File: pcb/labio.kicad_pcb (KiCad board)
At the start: 2 copper layers, 150 x 85 mm, 212 parts, among them IC201 AT24CS32-XHM, J701 JACK_TRRS_6PINS, P1 CONN_02X20, P301 CONN_01X04, P302 CONN_01X04, P303 CONN_01X04, P401 CONN_01X12, P601 CONN_01X02, P602 CONN_01X02, P603 CONN_01X04, P604 CONN_01X02, P605 CONN_01X03, P606 CONN_01X03, P607 CONN_01X05, P608 CONN_01X05, P701 CONN_01X04, P702 CONN_01X04, P703 CONN_01X04, P704 CONN_01X02, P901 CONN_01X06, Q301 PHOTOTRANSISTOR, Q302 Q_NMOS_GSD, Q303 Q_NMOS_GSD, Q601 Q_NMOS_GSD, Q602 Q_NMOS_GSD, Q603 Q_NMOS_GSD, Q604 Q_NMOS_GSD, Q605 Q_NMOS_GSD, Q606 Q_NMOS_GSD, Q607 Q_NMOS_GSD, Q608 Q_NMOS_GSD, Q609 Q_NMOS_GSD, Q610 Q_NMOS_GSD, Q611 Q_NMOS_GSD, Q612 Q_NMOS_GSD, Q613 Q_NMOS_GSD, SW301 DIP_SWITCH_X04, SW401 DIP_SWITCH_X04, SW501 DIP_SWITCH_X04, SW601 DIP_SWITCH_X04, SW602 DIP_SWITCH_X04, SW603 DIP_SWITCH_X04, SW604 DIP_SWITCH_X04, SW605 ROT_ENC, SW606 DIP_SWITCH_X04, SW701 DIP_SWITCH_X04, SW702 DIP_SWITCH_X04, SW801 SW_PUSH, SW802 SW_PUSH, SW803 SW_PUSH, SW804 SW_PUSH, SW805 SW_PUSH, U201 AP7365_SOT-23-5, U301 ADS1015, U501 LSM303D, U502 BMP280, U503 L3GD20H, U601 L298P_PowerSO20, U701 SPU0410HR5H, U702 WM8731

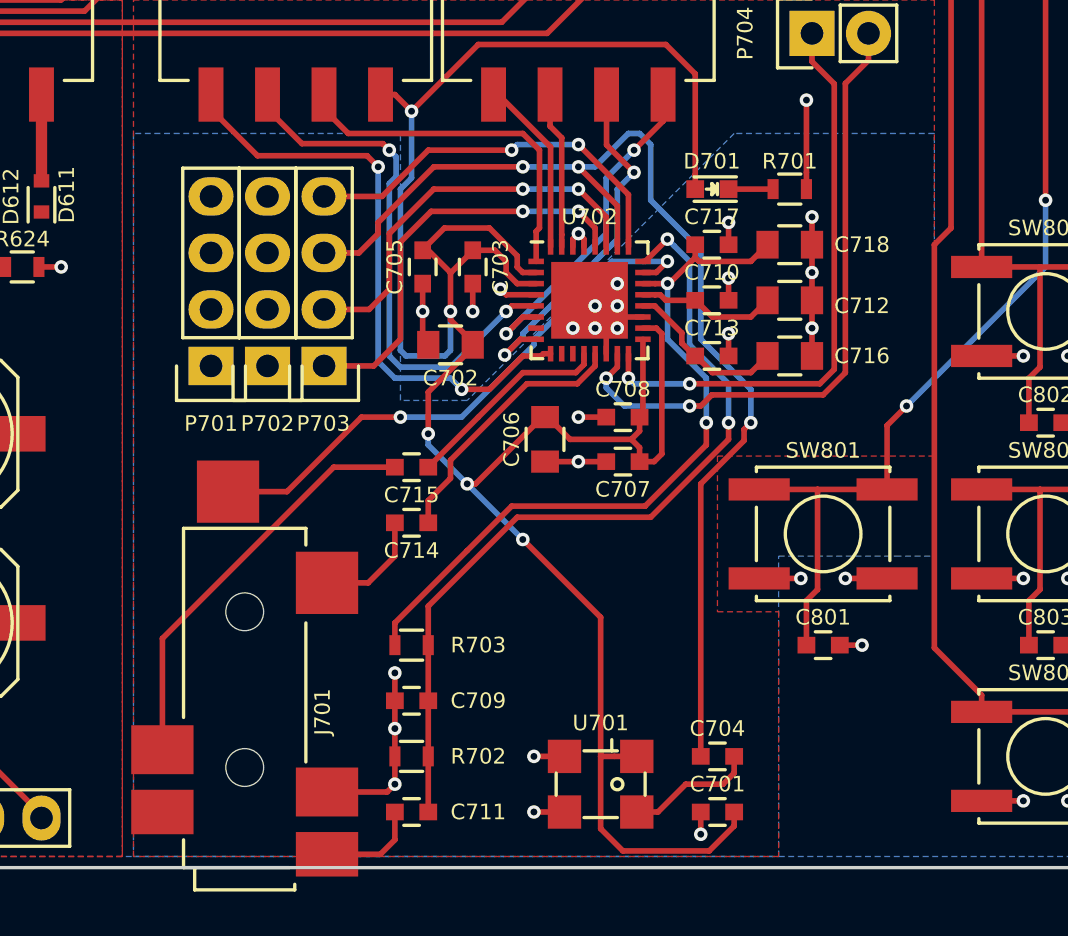
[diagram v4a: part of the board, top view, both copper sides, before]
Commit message: combine gnd and gnda nets per mixed signal layout suggestions from analog, ti
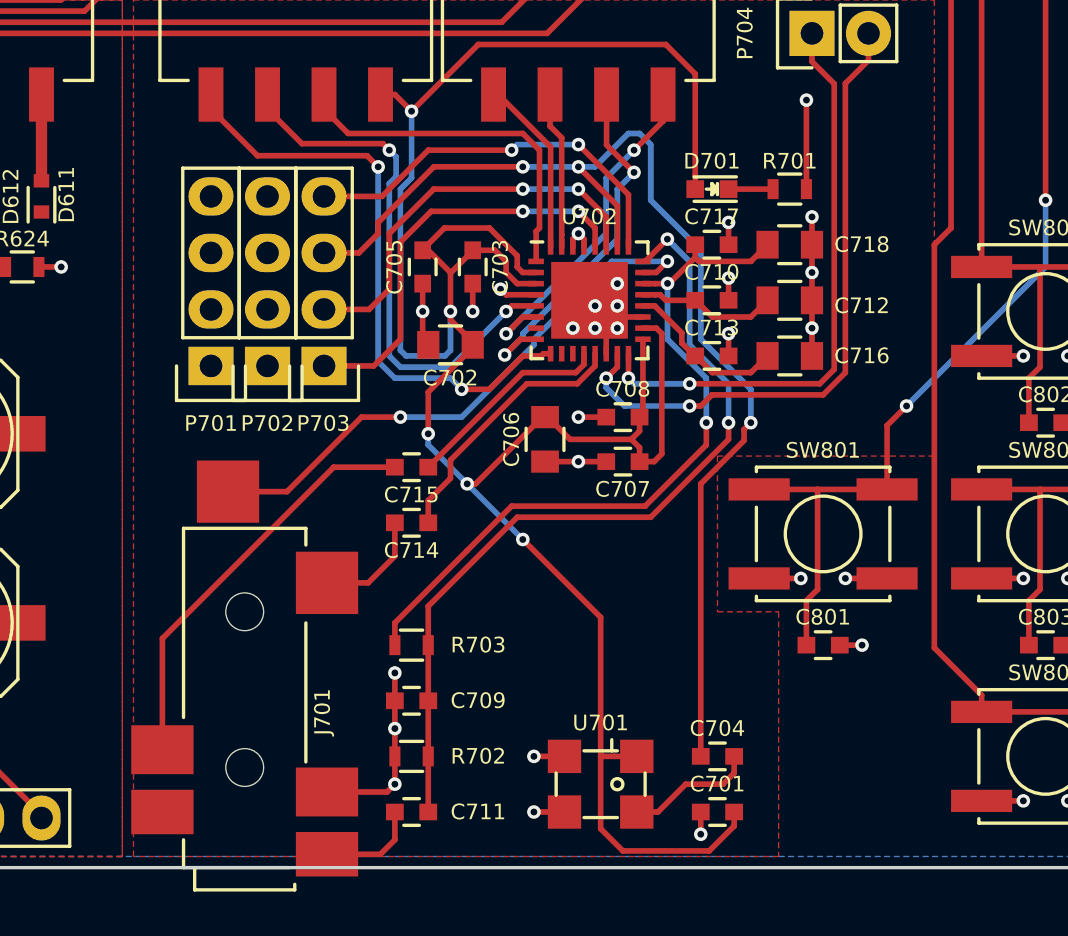
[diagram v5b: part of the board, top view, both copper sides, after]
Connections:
- C701 pad 1: GNDA -> GND
- C706 pad 2: GNDA -> GND
- C707 pad 2: GNDA -> GND
- C708 pad 2: GNDA -> GND
- C709 pad 2: GNDA -> GND
- C710 pad 2: GNDA -> GND
- C712 pad 2: GNDA -> GND
- C713 pad 2: GNDA -> GND
- C716 pad 2: GNDA -> GND
- C717 pad 2: GNDA -> GND
- C718 pad 2: GNDA -> GND
- J701 pad 4: GNDA -> GND
- P701 pad 1: GNDA -> GND
- P701 pad 2: GNDA -> GND
- P701 pad 3: GNDA -> GND
- P701 pad 4: GNDA -> GND
- R702 pad 2: GNDA -> GND
- U701 pad 2: GNDA -> GND
- U701 pad 3: GNDA -> GND
- U702 pad 14: GNDA -> GND
- U702 pad 19: GNDA -> GND
- U702 pad 33: GNDA -> GND
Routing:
- net GND: track 270.7 -> 309.2 mm, vias 181 -> 201
- net GNDA: track 38.5 -> 0.00 mm, vias 20 -> 0
- removed copper zone on B.Cu, net GNDA

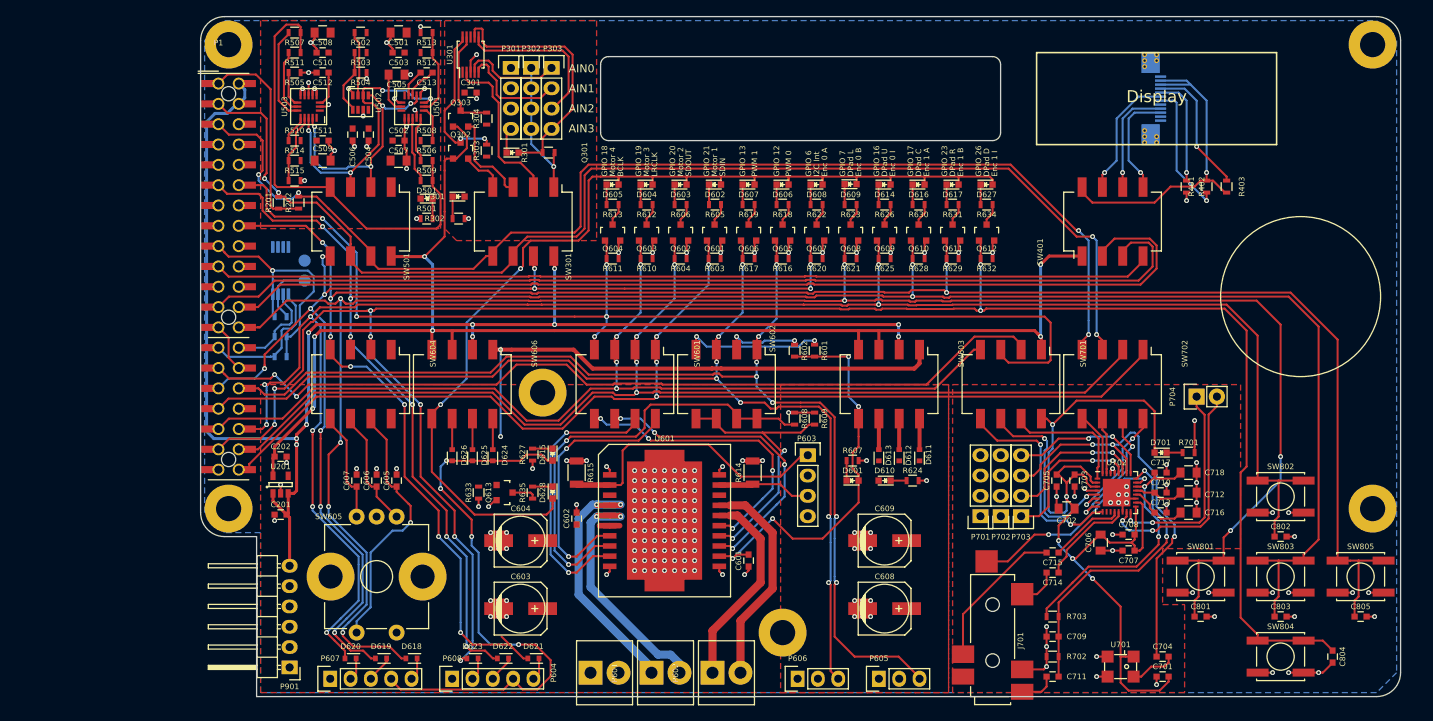
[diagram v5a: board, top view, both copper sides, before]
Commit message: expand outline to 175x85mm. move screen zif connector to top
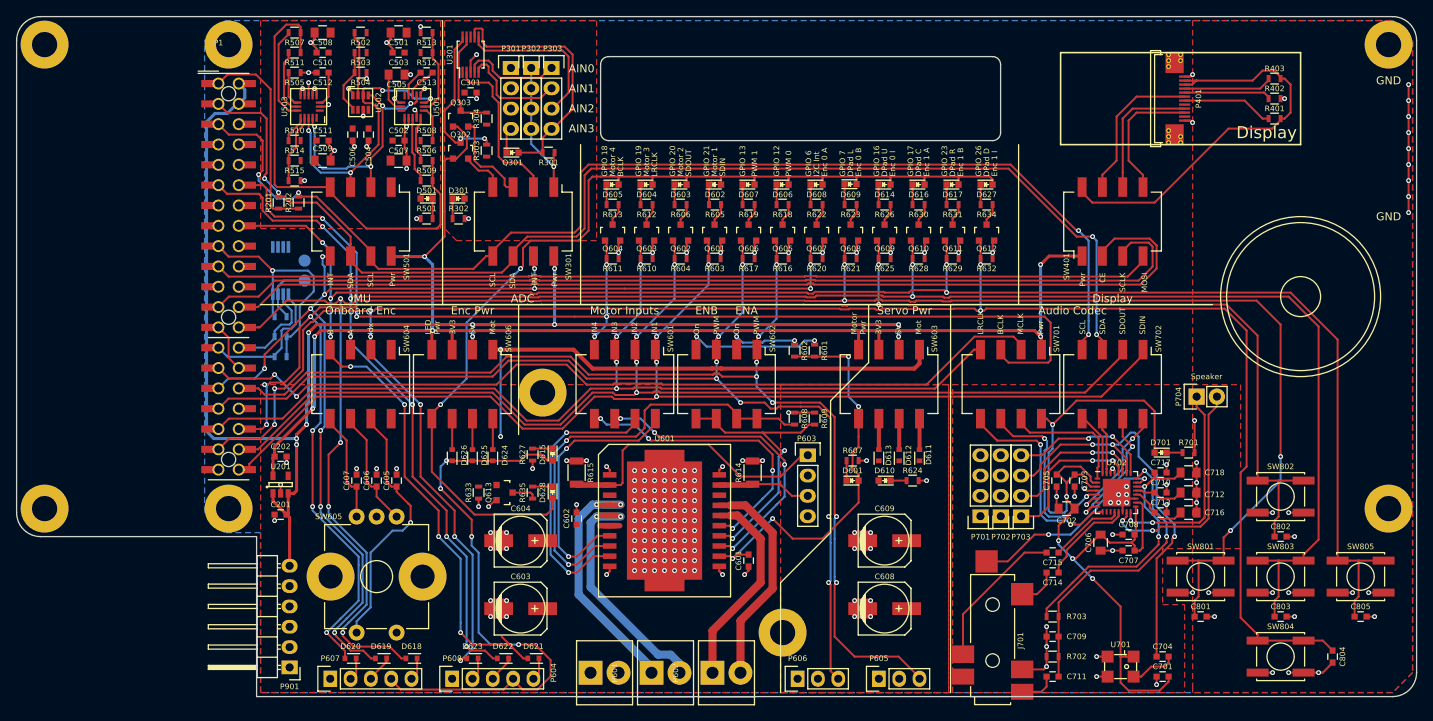
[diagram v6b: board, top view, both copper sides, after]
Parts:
- added H1007: hole, labio-special:hole-m3, F.Cu at (80.5, 53.5)
- added H1008: hole, labio-special:hole-m3, F.Cu at (80.5, 111.5)
- P401: value CONN_01X12 -> SFV12R-1ST__HLF; moved to F.Cu
- moved R402 15.6 mm to (234.2, 60.2), turned to 0 degrees
- moved R403 14.8 mm to (234.2, 57.8), turned to 0 degrees
- moved R401 12.0 mm to (234.2, 62.8), turned to 0 degrees
- moved P401 3.00 mm to (223.0, 60.2), turned to 270 degrees
- moved H1003 2.00 mm to (248.5, 53.5)
- moved H1004 2.00 mm to (248.5, 111.5)
- moved D301 0.25 mm to (132.2, 72.8)
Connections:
- P401 pad 10: Net-(P401-Pad10) -> /labio-display/OLED_MOSI
- P401 pad 11: Net-(P401-Pad10) -> (no net)
- P401 pad 2: (no net) -> Net-(P401-Pad2)
- P401 pad 3: /labio-display/OLED_MOSI -> Net-(P401-Pad2)
- P401 pad 4: /labio-display/OLED_SCK -> /labio-display/OLED_BS0
- P401 pad 5: (no net) -> /labio-display/OLED_BS1
- P401 pad 6: /labio-display/~OLED_RES -> /labio-display/~OLED_CS
- P401 pad 7: /labio-display/~OLED_CS -> /labio-display/~OLED_RES
- P401 pad 8: /labio-display/OLED_BS1 -> (no net)
- P401 pad 9: /labio-display/OLED_BS0 -> /labio-display/OLED_SCK
- R401 pad 2: Net-(P401-Pad10) -> Net-(P401-Pad2)
- R403 pad 2: Net-(P401-Pad10) -> Net-(P401-Pad2)
- SW401 pad 8: Net-(P401-Pad10) -> Net-(P401-Pad2)
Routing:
- net Net-(P401-Pad2): track 0.00 -> 51.9 mm
- net Net-(P401-Pad10): track 41.6 -> 0.00 mm, vias 1 -> 0
- net (no net): track 0.00 -> 16.0 mm, vias 0 -> 9
- net /labio-display/OLED_BS0: track 16.7 -> 11.1 mm, vias 1 -> 0
- net /labio-display/~OLED_RES: track 16.9 -> 11.4 mm, vias 1 -> 0
- net /labio-display/~OLED_CS: track 15.9 -> 19.1 mm, vias 1 -> 0
- net /labio-display/OLED_SCK: track 13.8 -> 16.9 mm, vias 1 -> 0
- net /labio-display/OLED_MOSI: track 13.6 -> 16.5 mm, vias 1 -> 0
- net /labio-display/OLED_BS1: track 13.7 -> 10.9 mm, vias 1 -> 0
- net GND: track 309.2 -> 310.9 mm, vias 201 -> 203
- added copper zone on F.Cu, net GND
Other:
- board size 150 x 85 mm -> 175 x 85 mm
- board text added: "3V3"
- board text added: "5V"
- board text added: "A"
- board text added: "ADC"
- board text added: "Audio Codec"
- board text added: "B"
- board text added: "CE"
- board text added: "ENA"
- board text added: "ENB"
- board text added: "Enc Pwr"
- board text added: "GND"
- board text added: "IMU"
- board text added: "IN1"
- board text added: "IN2"
- board text added: "IN3"
- board text added: "IN4"
- board text added: "INT"
- board text added: "Idx"
- board text added: "LED Pwr"
- board text added: "MCLK"
- board text added: "MOSI"
- board text added: "Mot"
- board text added: "Motor Inputs"
- board text added: "Motor Pwr"
- board text added: "On"
- board text added: "Onboard Enc"
- board text added: "PWM"
- board text added: "Pwr"
- board text added: "SCL"
- board text added: "SCLK"
- board text added: "SDA"
- board text added: "Servo Pwr"
- board text added: "Speaker"

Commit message: shrink board to 85x150mm with tab board under rpi 0/debugger
* use space under rpi 0/debugger for imu since no visibility is needed
* rearrange dpad buttons and speaker to be more compact
* use 3V3_EXTRA for i2c pullups for consistency
* add bottom right hole to match future power module
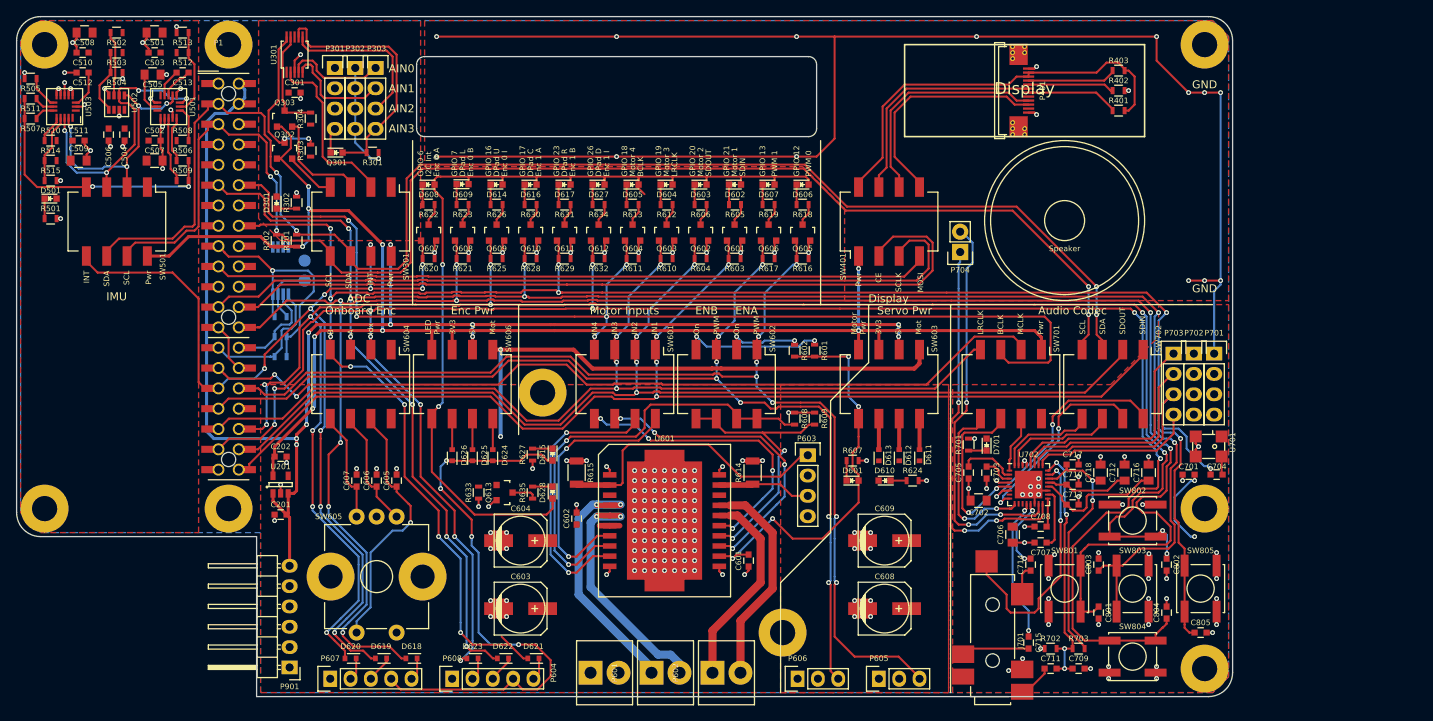
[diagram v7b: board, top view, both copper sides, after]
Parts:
- added H1009: hole, labio-special:hole-m3, F.Cu at (225.5, 131.5)
- moved D608 48.5 mm to (128.5, 71.0)
- moved D609 48.5 mm to (132.8, 71.0)
- moved D614 48.5 mm to (137.0, 71.0)
- moved D616 48.5 mm to (141.2, 71.0)
- moved D617 48.5 mm to (145.5, 71.0)
- moved D627 48.5 mm to (149.8, 71.0)
- moved Q607 48.5 mm to (128.5, 77.0)
- moved Q608 48.5 mm to (132.8, 77.0)
- moved Q609 48.5 mm to (137.0, 77.0)
- moved Q610 48.5 mm to (141.2, 77.0)
- moved Q611 48.5 mm to (145.5, 77.0)
- moved Q612 48.5 mm to (149.8, 77.0)
- moved R620 48.5 mm to (128.5, 80.2)
- moved R621 48.5 mm to (132.8, 80.2)
- moved R622 48.5 mm to (128.5, 73.5)
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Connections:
- R201 pad 1: /labio-rpi/3V3_1 -> /labio-rpi/3V3_EXTRA
- R202 pad 1: /labio-rpi/3V3_1 -> /labio-rpi/3V3_EXTRA
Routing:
- net GND: track 310.9 -> 506.9 mm, vias 203 -> 226
- net /labio-audio/VDD3V3_J: track 111.1 -> 32.3 mm, vias 5 -> 2
- net /labio-rpi/GPIO10_SPI0_MOSI: track 118.9 -> 91.0 mm
- net /labio-rpi/GPIO11_SPI0_SCLK: track 127.9 -> 100.3 mm
- net /labio-rpi/GPIO8_SPI0_CE0_N: track 128.3 -> 100.8 mm
- net /labio-rpi/GPIO1_SDA1: track 154.4 -> 181.4 mm
- net /labio-rpi/3V3_1: track 27.3 -> 1.31 mm
- net /labio-rpi/GPIO3_SCL1: track 150.5 -> 174.4 mm
- net /labio-imu/INT_J: track 57.8 -> 33.9 mm, vias 0 -> 2
- net /labio-adc/ALERT: track 149.2 -> 126.2 mm, vias 11 -> 10
- net /labio-audio/SPEAKER_L: track 26.2 -> 48.9 mm, vias 2 -> 3
- net /labio-rpi/3V3_EXTRA: track 170.9 -> 193.1 mm, vias 6 -> 9
- net /labio-audio/SPEAKER_R: track 29.1 -> 50.3 mm, vias 2 -> 3
- net /labio-dpad/DPAD_RIGHT: track 257.3 -> 239.2 mm, vias 9 -> 11
- net (no net): track 16.0 -> 0.00 mm, vias 9 -> 0
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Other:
- board size 175 x 85 mm -> 152 x 85 mm
- net class 10/10: clearance 0.254 -> 0.2032
- net class Motors: clearance 0.254 -> 0.2032
- net class Power: clearance 0.254 -> 0.2032

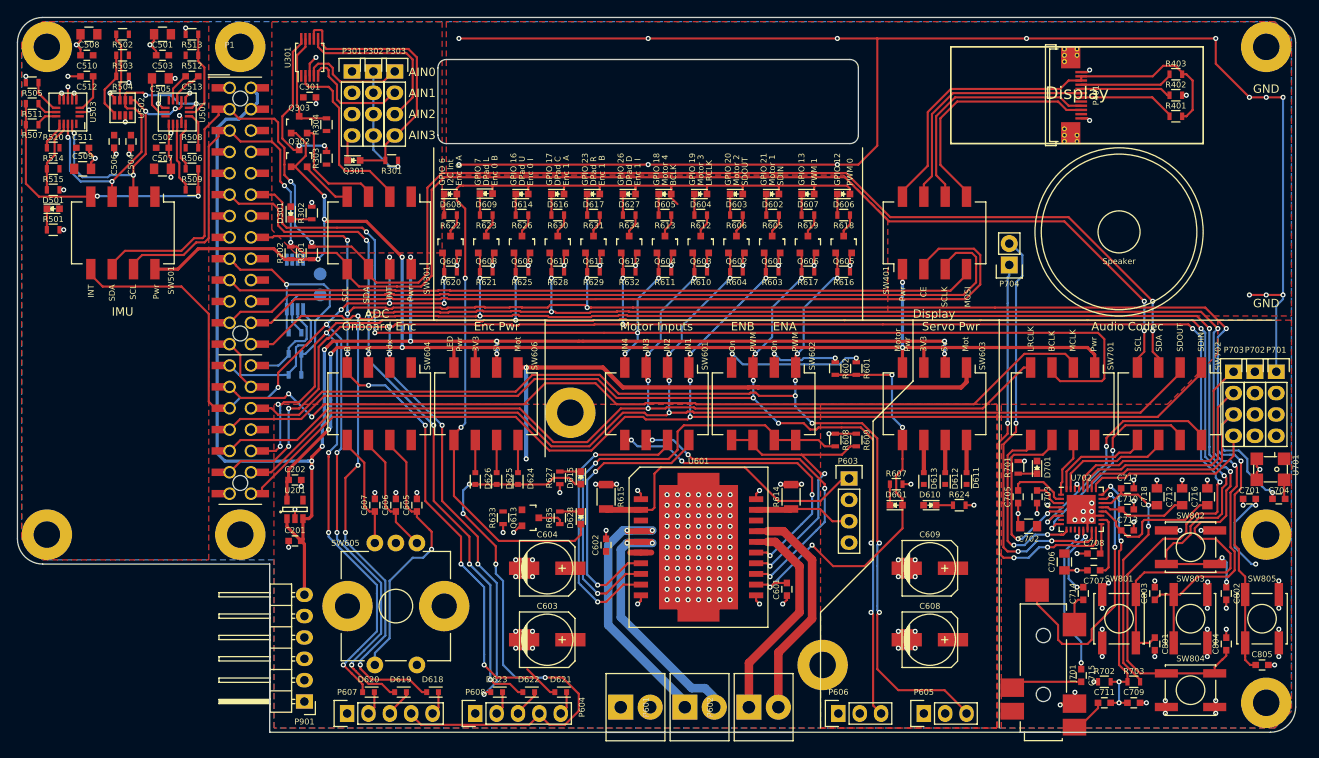
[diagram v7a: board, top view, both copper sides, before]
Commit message: add cmu + wise logos, clean up silk, review for final errors
* move audio jack in so copper pads are inside board
* add logos/identifier text on silk and copper
* change rpi connector for no paste (to be left depopulated at fab)
* change soldermask expansion to 2 mils/3 mils minimum width
* add labels for motor, ADC, codec headers
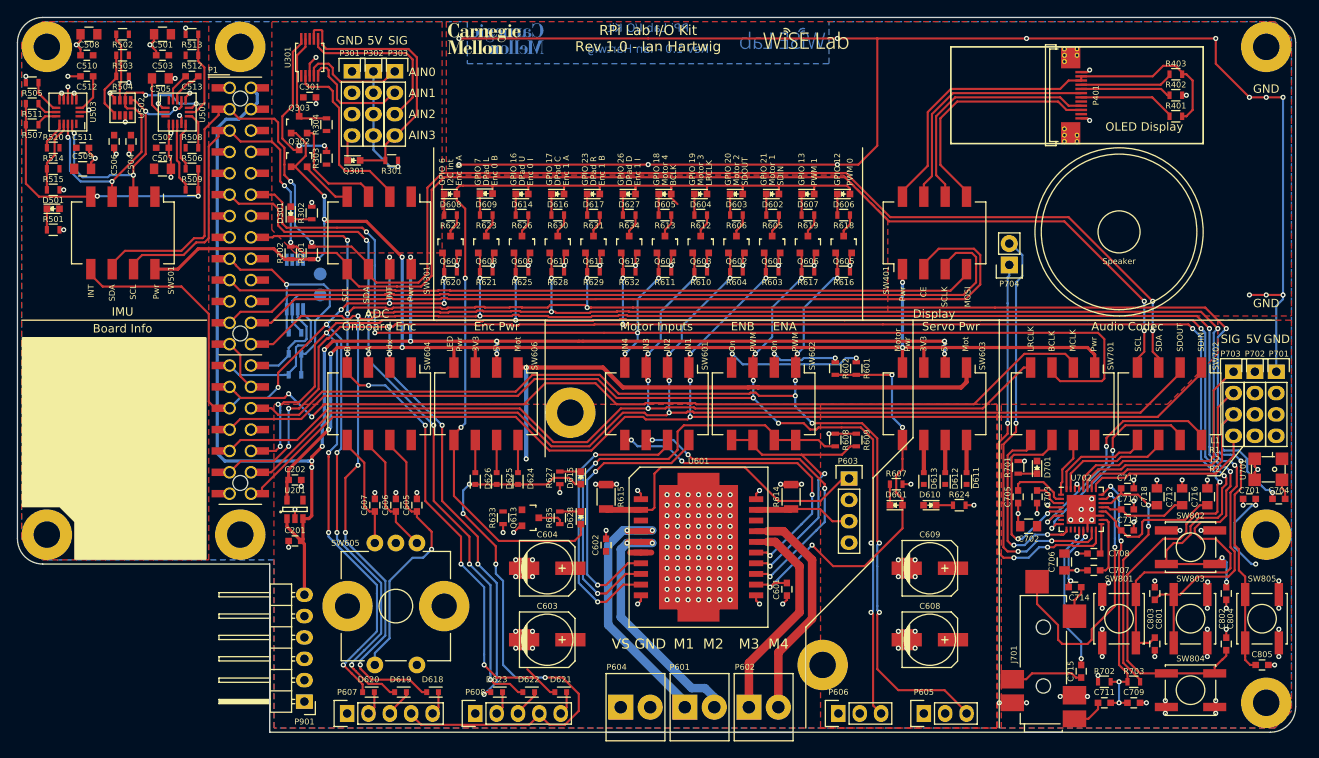
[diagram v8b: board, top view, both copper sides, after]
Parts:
- added G1: CMU_LOGO, labio-special:cmu_logo_fsilk_3.7mm, F.Cu at (132.5, 52.5)
- added G2: WISE_LOGO, labio-special:wise_logo_fsilk_2.5mm, F.Cu at (170.8, 52.5)
- added G3: CMU_LOGO, labio-special:cmu_logo_fcu_3.7mm, B.Cu at (135.2, 52.5)
- added G4: WISE_LOGO, labio-special:wise_logo_fcu_2.5mm, B.Cu at (168.0, 52.5)
- C512: value 0.01uF 25V -> 0.01uF-25V
- P1: footprint labio-special:Pin_Header_Straight_TH-SMT_2x20 -> labio-special:Pin_Header_Straight_TH-SMT-NoPaste_2x20
- moved C714 1.25 mm to (202.8, 117.8), turned to 180 degrees
- moved J701 1.00 mm to (199.0, 134.0)
- moved C715 0.50 mm to (203.5, 127.8)
- moved U701 0.26 mm to (225.8, 103.7)
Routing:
- net (no net): track 0.00 -> 3.25 mm, vias 0 -> 2
- net /labio-audio/TRRS_L_C: track 8.95 -> 7.99 mm
- net GND: track 506.9 -> 507.3 mm, vias 226 -> 225
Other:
- outline, holes or cut-outs redrawn
- rule pad_to_mask_clearance: 0.2 -> 0.051
- board text added: "Board Info"
- board text added: "CUTOUT"
- board text added: "L1 R1 L2 R2"
- board text added: "M1"
- board text added: "M2"
- board text added: "M3"
- board text added: "M4"
- board text added: "OLED Display"
- board text added: "RPi Lab I/O Kit"
- board text added: "RPi Lab I/O Kit Rev 1.0 - Ian Hartwig"
- board text added: "Rev 1.0 - Ian Hartwig"
- board text added: "SIG"
- board text added: "VS"
